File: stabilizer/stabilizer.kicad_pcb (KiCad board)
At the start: 2 copper layers, 38.1 x 20.2 mm, 3 parts

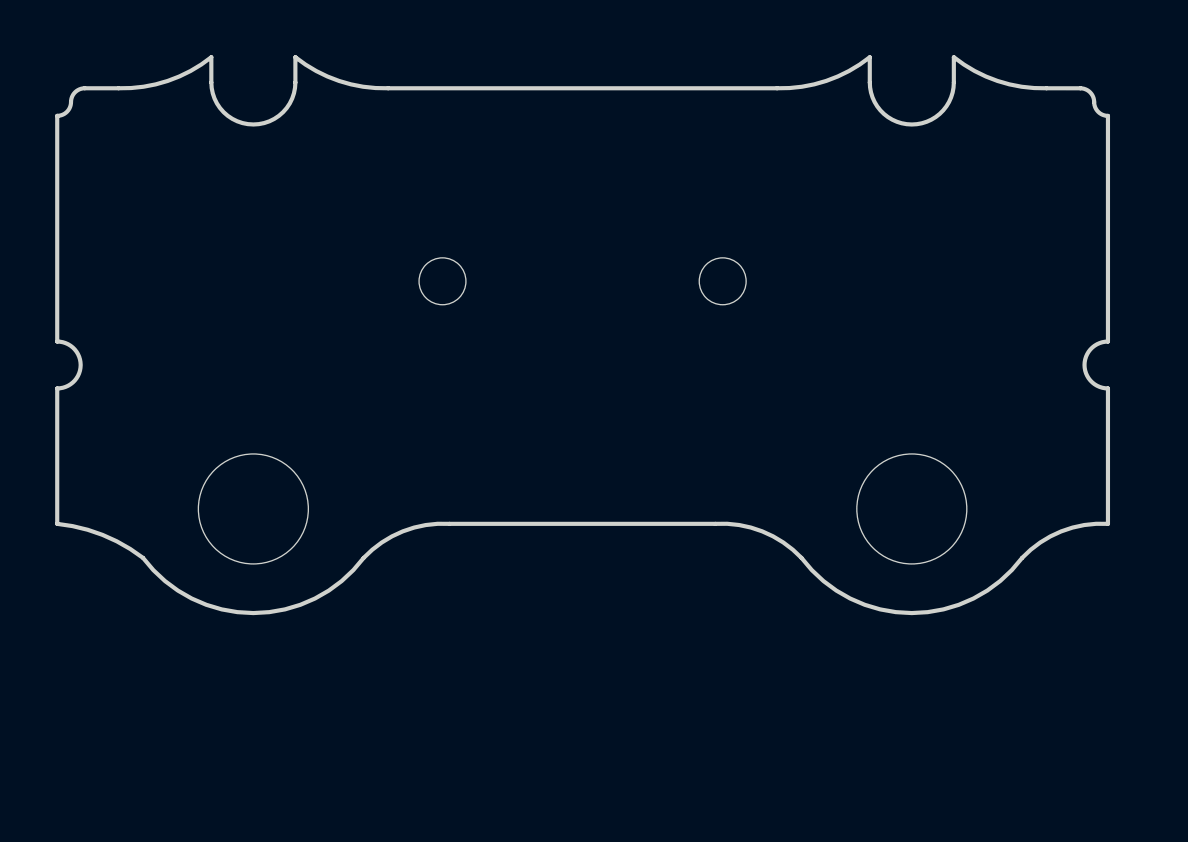
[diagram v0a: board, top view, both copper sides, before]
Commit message: tweak stabilizer to match 1u
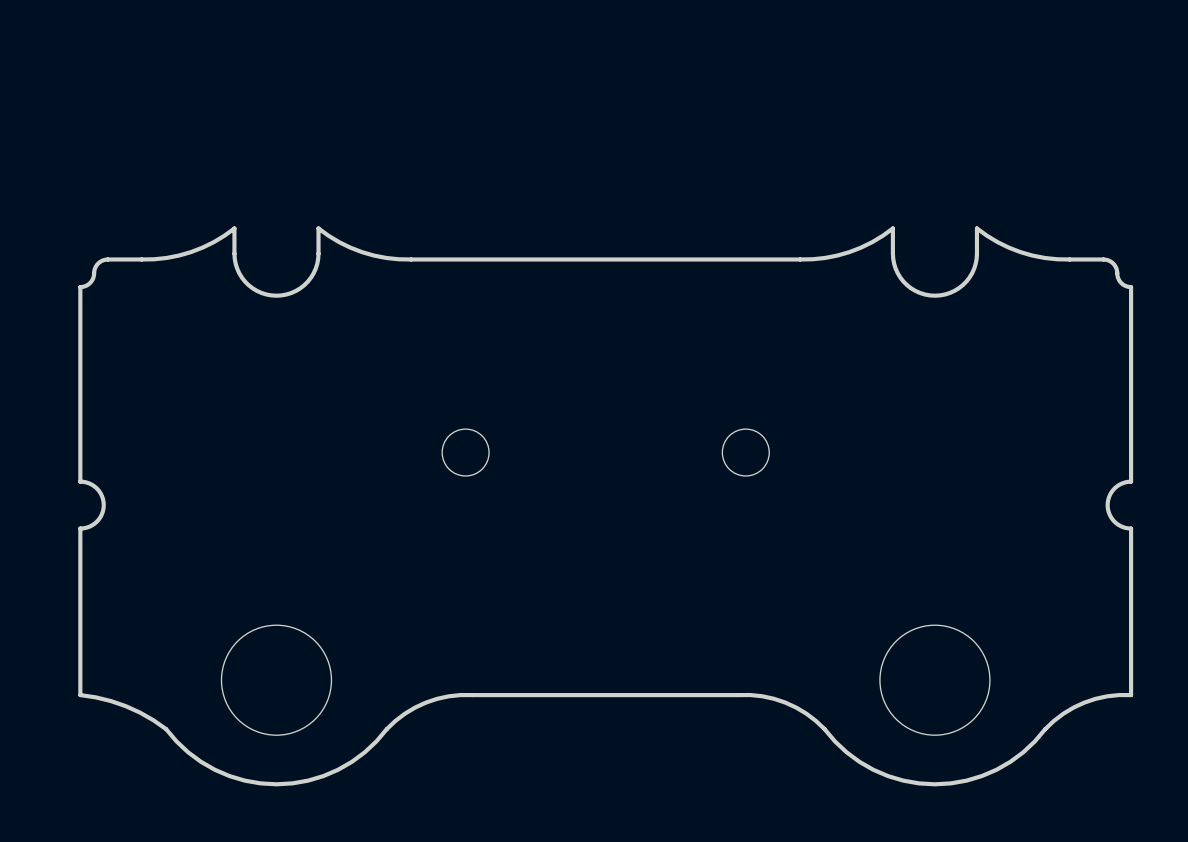
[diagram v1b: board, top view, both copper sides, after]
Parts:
- moved ? 6.27 mm to (191.1, 131.3)
- moved SW 6.27 mm to (203.0, 123.0)
- moved ? 6.27 mm to (214.9, 131.3)
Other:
- outline, holes or cut-outs redrawn
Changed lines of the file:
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@@
   (net 0 "")
   (footprint "" (layer "F.Cu")
-    (at 214.0997 125.0457)
+    (at 214.938 131.255)
     (fp_text reference "" (at 0 -0.225) (layer "F.SilkS")
         (effects (font (size 1.27 1.27) (thickness 0.15)))
@@
   )
   (footprint "Button_Switch_Keyboard:SW_Lekker_MX_1.00u_PCB" (layer "F.Cu")
-    (at 202.1617 116.7907 180)
+    (at 203 123 180)
     (descr "Cherry MX keyswitch, 1.00u, PCB mount, http://cherryamericas.com/wp-content/uploads/2014/12/mx_cat.pdf")
     (tags "Cherry MX keyswitch 1.00u PCB")
@@
   )
   (footprint "" (layer "F.Cu")
-    (at 190.2237 125.0457)
+    (at 191.062 131.255)
     (fp_text reference "" (at 0 -0.225) (layer "F.SilkS")
         (effects (font (size 1.27 1.27) (thickness 0.15)))
@@
     (pad "" np_thru_hole circle (at 0 0) (size 3.9878 3.9878) (drill 3.9878) (layers "*.Cu" "*.Mask"))
   )
-  (gr_arc (start 221.2117 110.792307) (mid 220.858145 110.645862) (end 220.7117 110.292307)
+  (gr_arc (start 222.05 117.001607) (mid 221.696444 116.855161) (end 221.55 116.501607)
     (stroke (width 0.15) (type default)) (layer "Edge.Cuts"))
-  (gr_arc (start 194.2237 126.8207) (mid 195.642792 125.858208) (end 197.3357 125.585667)
+  (gr_arc (start 195.062 133.03) (mid 196.48109 132.067495) (end 198.174 131.794967)
     (stroke (width 0.15) (type default)) (layer "Edge.Cuts"))
-  (gr_arc (start 220.2117 109.792307) (mid 220.565252 109.938755) (end 220.7117 110.292307)
+  (gr_arc (start 221.05 116.001607) (mid 221.403551 116.148054) (end 221.55 116.501607)
     (stroke (width 0.15) (type default)) (layer "Edge.Cuts"))
-  (gr_line (start 212.5757 108.665992) (end 212.5757 109.580992)
+  (gr_line (start 213.414 114.874445) (end 213.414 115.789445)
     (stroke (width 0.15) (type default)) (layer "Edge.Cuts"))
-  (gr_arc (start 188.6997 108.6657) (mid 187.118066 109.525281) (end 185.3377 109.791255)
+  (gr_arc (start 189.538 114.874445) (mid 187.956367 115.734029) (end 186.176 116)
     (stroke (width 0.15) (type default)) (layer "Edge.Cuts"))
-  (gr_line (start 215.623697 108.665992) (end 215.6237 109.580992)
+  (gr_line (start 216.461997 114.874445) (end 216.462 115.789445)
     (stroke (width 0.15) (type default)) (layer "Edge.Cuts"))
-  (gr_line (start 218.9862 109.791547) (end 220.2117 109.792307)
+  (gr_line (start 219.8245 116) (end 221.05 116)
     (stroke (width 0.15) (type default)) (layer "Edge.Cuts"))
-  (gr_arc (start 195.1102 109.791255) (mid 193.329584 109.525321) (end 191.747697 108.6657)
+  (gr_line (start 222.05 117.001607) (end 222.05 124.056607)
     (stroke (width 0.15) (type default)) (layer "Edge.Cuts"))
-  (gr_line (start 183.1117 110.791255) (end 183.1117 118.9757)
+  (gr_arc (start 195.9485 116) (mid 194.167886 115.734061) (end 192.585997 114.874445)
     (stroke (width 0.15) (type default)) (layer "Edge.Cuts"))
-  (gr_arc (start 183.1117 125.585667) (mid 184.754206 125.985209) (end 186.2237 126.8207)
+  (gr_arc (start 183.95 131.794967) (mid 185.592506 132.194509) (end 187.062 133.03)
     (stroke (width 0.15) (type default)) (layer "Edge.Cuts"))
-  (gr_arc (start 183.1117 118.9757) (mid 183.9617 119.8257) (end 183.1117 120.6757)
+  (gr_arc (start 183.95 124.055555) (mid 184.8 124.905555) (end 183.95 125.755555)
     (stroke (width 0.15) (type default)) (layer "Edge.Cuts"))
-  (gr_arc (start 218.0997 126.8207) (mid 214.0997 128.8207) (end 210.0997 126.8207)
+  (gr_arc (start 218.938 133.03) (mid 214.938 135.03) (end 210.938 133.03)
     (stroke (width 0.15) (type default)) (layer "Edge.Cuts"))
-  (gr_arc (start 206.974947 125.585667) (mid 208.67423 125.856796) (end 210.0997 126.8207)
+  (gr_arc (start 207.813247 131.794967) (mid 209.512522 132.066107) (end 210.938 133.03)
     (stroke (width 0.15) (type default)) (layer "Edge.Cuts"))
-  (gr_line (start 184.1117 109.791255) (end 185.3377 109.791255)
+  (gr_line (start 184.95 115.999445) (end 186.176 115.999445)
     (stroke (width 0.15) (type default)) (layer "Edge.Cuts"))
-  (gr_arc (start 218.0997 126.8207) (mid 219.518792 125.858208) (end 221.2117 125.585667)
+  (gr_arc (start 218.938 133.03) (mid 220.35709 132.067495) (end 222.05 131.794967)
     (stroke (width 0.15) (type default)) (layer "Edge.Cuts"))
-  (gr_line (start 195.1102 109.791255) (end 209.213708 109.791255)
+  (gr_line (start 195.9485 116) (end 210.052008 116)
     (stroke (width 0.15) (type default)) (layer "Edge.Cuts"))
-  (gr_arc (start 215.6237 109.580992) (mid 214.0997 111.104992) (end 212.5757 109.580992)
+  (gr_arc (start 216.462 115.789445) (mid 214.938 117.313445) (end 213.414 115.789445)
     (stroke (width 0.15) (type default)) (layer "Edge.Cuts"))
-  (gr_line (start 221.2117 125.585667) (end 221.2117 120.6757)
+  (gr_line (start 222.05 131.794967) (end 222.05 125.756607)
     (stroke (width 0.15) (type default)) (layer "Edge.Cuts"))
-  (gr_arc (start 212.5757 108.665992) (mid 210.994025 109.52537) (end 209.213708 109.791255)
+  (gr_arc (start 213.414 114.874445) (mid 211.832325 115.73382) (end 210.052008 115.999708)
     (stroke (width 0.15) (type default)) (layer "Edge.Cuts"))
-  (gr_line (start 197.3357 125.585667) (end 206.974947 125.585667)
+  (gr_line (start 198.174 131.794967) (end 207.813247 131.794967)
     (stroke (width 0.15) (type default)) (layer "Edge.Cuts"))
-  (gr_line (start 191.747697 108.6657) (end 191.7477 109.5807)
+  (gr_line (start 192.585997 114.874445) (end 192.586 115.789445)
     (stroke (width 0.15) (type default)) (layer "Edge.Cuts"))
-  (gr_arc (start 183.6117 110.291255) (mid 183.465275 110.64483) (end 183.1117 110.791255)
+  (gr_arc (start 184.45 116.500555) (mid 184.303563 116.854102) (end 183.95 117.000555)
     (stroke (width 0.15) (type default)) (layer "Edge.Cuts"))
-  (gr_arc (start 218.9862 109.791547) (mid 217.205584 109.525612) (end 215.623697 108.665992)
+  (gr_line (start 183.95 117.000555) (end 183.95 124.055555)
     (stroke (width 0.15) (type default)) (layer "Edge.Cuts"))
-  (gr_line (start 188.699697 108.6657) (end 188.6997 109.5807)
+  (gr_arc (start 219.8245 116) (mid 218.043887 115.734061) (end 216.461997 114.874445)
     (stroke (width 0.15) (type default)) (layer "Edge.Cuts"))
-  (gr_arc (start 191.7477 109.5807) (mid 190.2237 111.1047) (end 188.6997 109.5807)
+  (gr_line (start 189.537997 114.874445) (end 189.538 115.789445)
     (stroke (width 0.15) (type default)) (layer "Edge.Cuts"))
-  (gr_arc (start 194.2237 126.8207) (mid 190.2237 128.8207) (end 186.2237 126.8207)
+  (gr_arc (start 192.586 115.789445) (mid 191.062 117.313445) (end 189.538 115.789445)
     (stroke (width 0.15) (type default)) (layer "Edge.Cuts"))
-  (gr_line (start 183.1117 125.585667) (end 183.1117 120.6757)
+  (gr_arc (start 195.062 133.03) (mid 191.062 135.03) (end 187.062 133.03)
     (stroke (width 0.15) (type default)) (layer "Edge.Cuts"))
-  (gr_arc (start 221.2117 120.6757) (mid 220.3617 119.8257) (end 221.2117 118.9757)
+  (gr_line (start 183.95 131.794967) (end 183.95 125.755555)
     (stroke (width 0.15) (type default)) (layer "Edge.Cuts"))
-  (gr_arc (start 183.6117 110.291255) (mid 183.758169 109.937724) (end 184.1117 109.791255)
+  (gr_arc (start 222.05 125.756607) (mid 221.2 124.906607) (end 222.05 124.056607)
     (stroke (width 0.15) (type default)) (layer "Edge.Cuts"))
-  (gr_line (start 221.2117 110.792307) (end 221.2117 118.9757)
+  (gr_arc (start 184.45 116.500555) (mid 184.596456 116.146995) (end 184.95 116.000555)
     (stroke (width 0.15) (type default)) (layer "Edge.Cuts"))
 )
